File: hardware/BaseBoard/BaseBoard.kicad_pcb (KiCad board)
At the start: 2 copper layers, 81.3 x 106.7 mm, 89 parts, among them IC1 PCF8574RGTR, J1-ESP1 ESP-1-L, J1-ESP2 ESP-1-L, J1-ESP3 ESP-1-L, J1-ESP4 ESP-1-L, J1-ESP5 ESP-1-L, J1-ESP6 ESP-1-L, J1-ESP7 ESP-1-L, J1-ESP8 ESP-1-L, J2-ESP1 ESP-1-R, J2-ESP2 ESP-1-R, J2-ESP3 ESP-1-R, J2-ESP4 ESP-1-R, J2-ESP5 ESP-1-R, J2-ESP6 ESP-1-R, J2-ESP7 ESP-1-R, J2-ESP8 ESP-1-R, J3-BUS1 BUS-IN, J3-BUS2 BUS-IN, J3-BUS3 BUS-IN, J3-BUS4 BUS-IN, J3-BUS5 BUS-IN, J3-BUS6 BUS-IN, J3-BUS7 BUS-IN, J3-BUS8 BUS-IN, J4-BUS1 BUS-OUT, J4-BUS2 BUS-OUT, J4-BUS3 BUS-OUT, J4-BUS4 BUS-OUT, J4-BUS5 BUS-OUT, J4-BUS6 BUS-OUT, J4-BUS7 BUS-OUT, J4-BUS8 BUS-OUT, Q11 2N3904, Q12 AO3401A, Q21 2N3904, Q22 AO3401A, Q31 2N3904, Q32 AO3401A, Q41 2N3904, Q42 AO3401A, Q51 2N3904, Q52 AO3401A, Q61 2N3904, Q62 AO3401A, Q71 2N3904, Q72 AO3401A, Q81 2N3904, Q82 AO3401A, SW1 SW_DIP_SPSTx03, U1 AMS1117-3.3

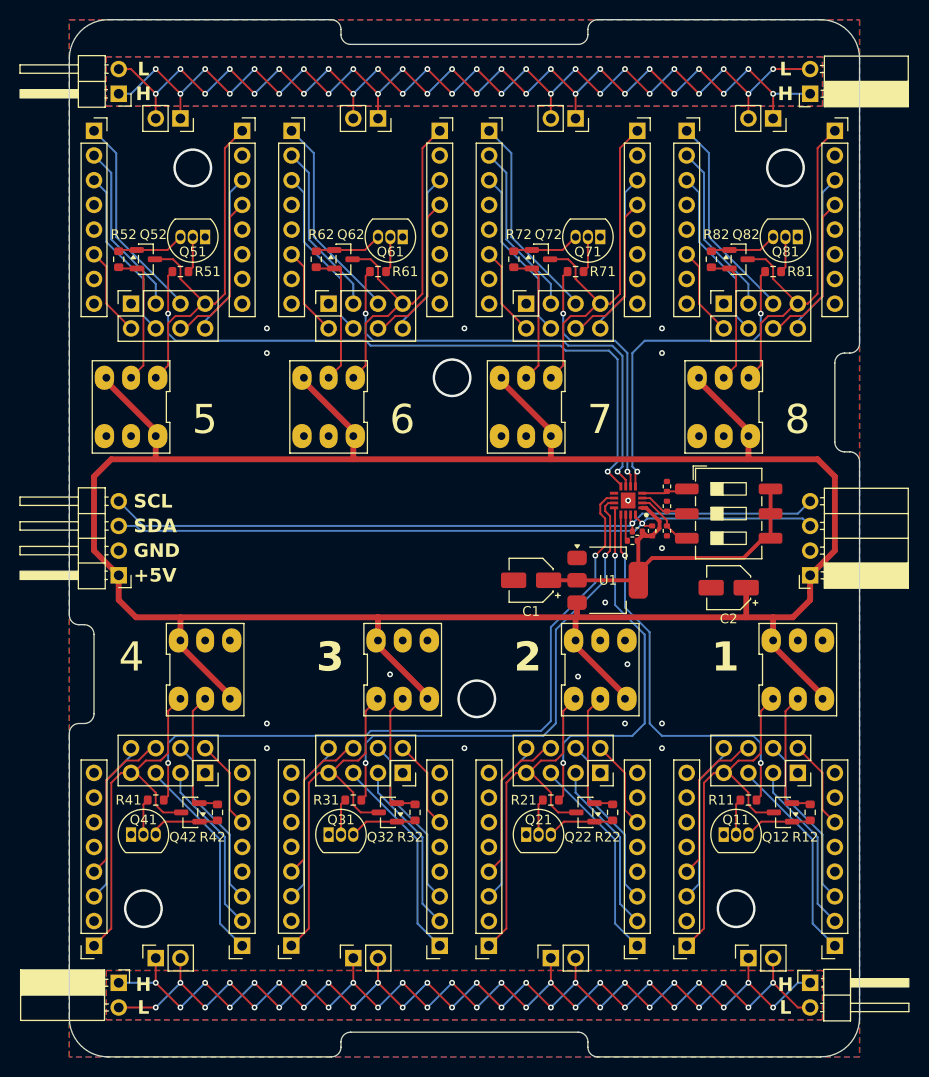
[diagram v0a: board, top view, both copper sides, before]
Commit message: Simplified BaseBoard.
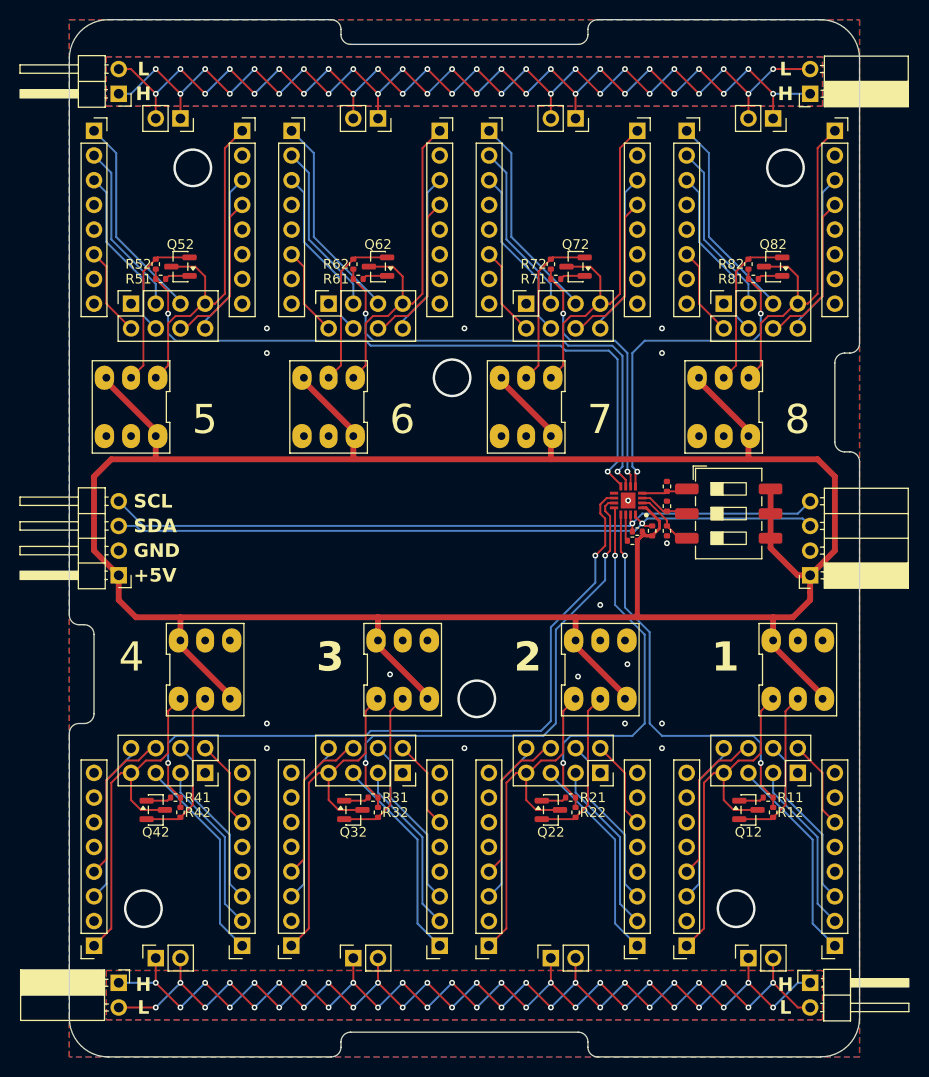
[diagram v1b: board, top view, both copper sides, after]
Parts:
- removed C1: 22µF, Capacitor_SMD:CP_Elec_4x5.3
- removed C2: 10µF, Capacitor_SMD:CP_Elec_4x5.3
- removed Q11, Q21, Q31, Q41, Q51, Q61, Q71, Q81: 2N3904, Package_TO_SOT_THT:TO-92_Inline
- removed U1: AMS1117-3.3, Package_TO_SOT_SMD:SOT-223-3_TabPin2
- R11, R21, R31, R41, R51, R61, R71, R81: value 500 -> 150; footprint Resistor_SMD:R_0603_1608Metric -> Resistor_SMD:R_0402_1005Metric
- R12, R22, R32, R42, R52, R62, R72, R82: value 500 -> 10k; footprint Resistor_SMD:R_0603_1608Metric -> Resistor_SMD:R_0402_1005Metric
- moved R52 3.84 mm to (130.8, 44.2), turned to -90 degrees
- moved R62 3.84 mm to (151.1, 44.2), turned to -90 degrees
- moved R72 3.84 mm to (171.4, 44.2), turned to -90 degrees
- moved R82 3.84 mm to (191.8, 44.2), turned to -90 degrees
- moved R12 3.81 mm to (194.3, 100.6), turned to 90 degrees
- moved R22 3.81 mm to (174.0, 100.6), turned to 90 degrees
- moved R32 3.81 mm to (153.7, 100.6), turned to 90 degrees
- moved R42 3.81 mm to (133.3, 100.6), turned to 90 degrees
- moved Q72 3.64 mm to (174.0, 44.5), turned to 180 degrees
- moved Q82 3.64 mm to (194.3, 44.5), turned to 180 degrees
- moved Q52 3.64 mm to (133.3, 44.5), turned to 180 degrees
- moved Q62 3.64 mm to (153.7, 44.5), turned to 180 degrees
- moved Q22 3.57 mm to (171.4, 100.3), turned to 0 degrees
- moved Q32 3.57 mm to (151.1, 100.3), turned to 0 degrees
- moved Q42 3.57 mm to (130.8, 100.3), turned to 0 degrees
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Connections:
- IC1 pad 1: +3V3 -> +5V
- Q12 pad 1: Net-(Q11-C) -> Net-(Q12-G)
- Q22 pad 1: Net-(Q21-C) -> Net-(Q22-G)
- Q32 pad 1: Net-(Q31-C) -> Net-(Q32-G)
- Q42 pad 1: Net-(Q41-C) -> Net-(Q42-G)
- Q52 pad 1: Net-(Q51-C) -> Net-(Q52-G)
- Q62 pad 1: Net-(Q61-C) -> Net-(Q62-G)
- Q72 pad 1: Net-(Q71-C) -> Net-(Q72-G)
- Q82 pad 1: Net-(Q81-C) -> Net-(Q82-G)
- R1 pad 2: +3V3 -> +5V
- R11 pad 1: Net-(Q11-B) -> Net-(Q12-G)
- R12 pad 2: Net-(Q11-C) -> SWPIN-ESP1
- R2 pad 2: +3V3 -> +5V
- R21 pad 1: Net-(Q21-B) -> Net-(Q22-G)
- R22 pad 2: Net-(Q21-C) -> SWPIN-ESP2
- R3 pad 2: +3V3 -> +5V
- R31 pad 1: Net-(Q31-B) -> Net-(Q32-G)
- R32 pad 2: Net-(Q31-C) -> SWPIN-ESP3
- R41 pad 1: Net-(Q41-B) -> Net-(Q42-G)
- R42 pad 2: Net-(Q41-C) -> SWPIN-ESP4
- R51 pad 1: Net-(Q51-B) -> Net-(Q52-G)
- R52 pad 2: Net-(Q51-C) -> SWPIN-ESP5
- R61 pad 1: Net-(Q61-B) -> Net-(Q62-G)
- R62 pad 2: Net-(Q61-C) -> SWPIN-ESP6
- R71 pad 1: Net-(Q71-B) -> Net-(Q72-G)
- R72 pad 2: Net-(Q71-C) -> SWPIN-ESP7
- R81 pad 1: Net-(Q81-B) -> Net-(Q82-G)
- R82 pad 2: Net-(Q81-C) -> SWPIN-ESP8
- SW1 pad 4: +3V3 -> +5V
- SW1 pad 5: +3V3 -> +5V
- SW1 pad 6: +3V3 -> +5V
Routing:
- net +3V3: track 42.6 -> 0.00 mm
- net +5V: track 266.4 -> 289.2 mm
- net Net-(Q41-C): track 7.25 -> 0.00 mm
- net Net-(Q71-C): track 6.96 -> 0.00 mm
- net Net-(Q21-C): track 6.96 -> 0.00 mm
- net Net-(Q61-C): track 6.96 -> 0.00 mm
- net Net-(Q51-C): track 6.96 -> 0.00 mm
- net Net-(Q11-C): track 6.96 -> 0.00 mm
- net Net-(Q81-C): track 6.96 -> 0.00 mm
- net Net-(Q31-C): track 6.96 -> 0.00 mm
- net Net-(Q41-B): track 3.74 -> 0.00 mm
- net Net-(Q81-B): track 3.74 -> 0.00 mm
- net Net-(Q31-B): track 3.74 -> 0.00 mm
- net Net-(Q21-B): track 3.74 -> 0.00 mm
- net Net-(Q11-B): track 3.74 -> 0.00 mm
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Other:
- board text added: "COMChallange Baseboard v1.1 github.com/raphweb"
- board text removed: "COMChallange Baseboard v1.1 - github.com/raphweb"

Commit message: Minor BaseBoard updates.
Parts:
- added R7: 50, Resistor_SMD:R_0603_1608Metric, F.Cu at (181.6, 74.2)
- renumbered Q12 to Q1, Q22 to Q2, Q32 to Q3, Q42 to Q4, Q52 to Q5, Q62 to Q6, Q72 to Q7, Q82 to Q8
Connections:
- IC1 pad 1: +5V -> +5VSwitching
- R1 pad 2: +5V -> +5VSwitching
- R2 pad 2: +5V -> +5VSwitching
- R3 pad 2: +5V -> +5VSwitching
- SW1 pad 4: +5V -> +5VSwitching
- SW1 pad 5: +5V -> +5VSwitching
- SW1 pad 6: +5V -> +5VSwitching
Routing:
- net +5VSwitching: track 0.00 -> 27.5 mm
- net +5V: track 289.2 -> 267.3 mm

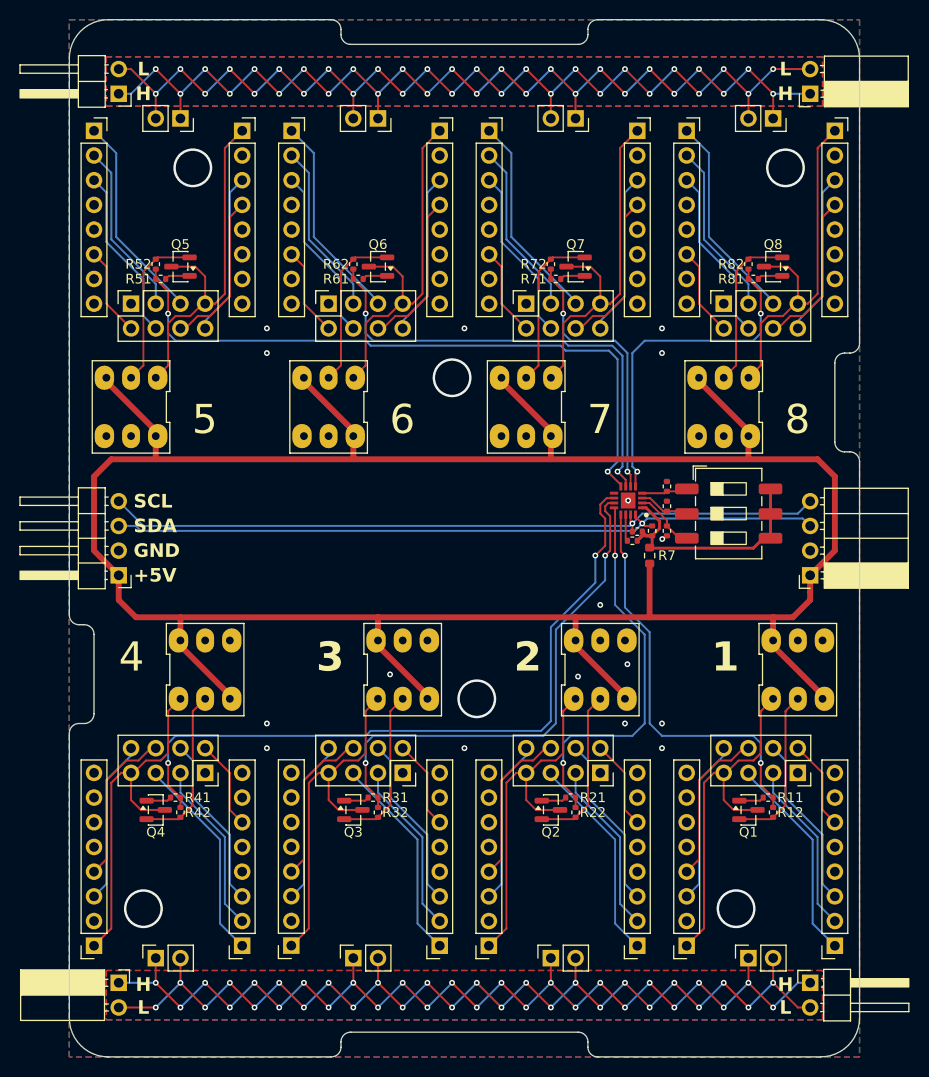
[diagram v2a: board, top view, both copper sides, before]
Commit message: Larger resistors and more GND vias.
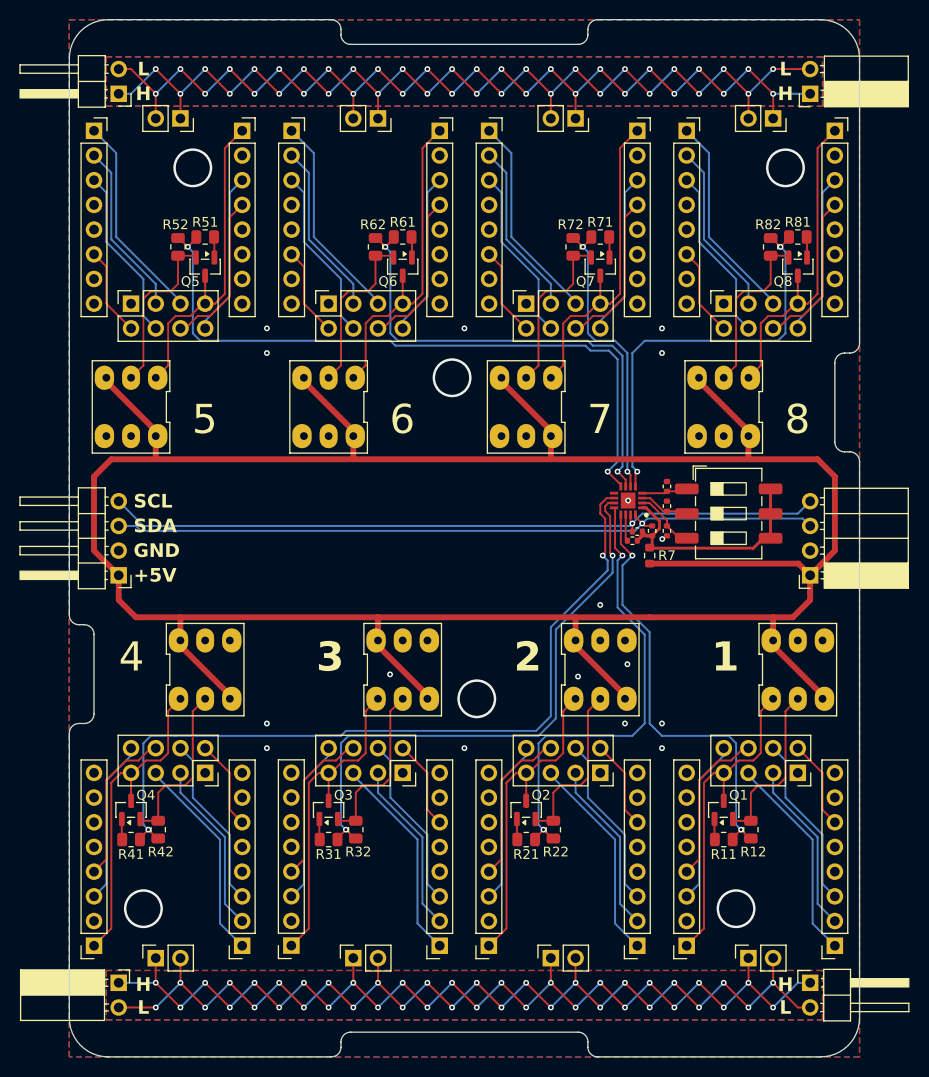
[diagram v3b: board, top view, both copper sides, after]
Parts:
- R11, R12, R21, R22, R31, R32, R41, R42, R51, R52, R61, R62, R71, R72, R81, R82: footprint Resistor_SMD:R_0402_1005Metric -> Resistor_SMD:R_0805_2012Metric
- moved R11 6.29 mm to (189.2, 103.4)
- moved R21 6.29 mm to (168.9, 103.4)
- moved R31 6.29 mm to (148.6, 103.4)
- moved R41 6.29 mm to (128.3, 103.4)
- moved R61 6.29 mm to (156.2, 41.4)
- moved R71 6.29 mm to (176.5, 41.4)
- moved R81 6.29 mm to (196.8, 41.4)
- moved R51 6.29 mm to (135.9, 41.4)
- moved R52 2.90 mm to (133.1, 42.4), turned to 90 degrees
- moved R62 2.90 mm to (153.4, 42.4), turned to 90 degrees
- moved R72 2.90 mm to (173.7, 42.4), turned to 90 degrees
- moved R82 2.90 mm to (194.1, 42.4), turned to 90 degrees
- moved R12 2.90 mm to (192.0, 102.4), turned to -90 degrees
- moved R22 2.90 mm to (171.7, 102.4), turned to -90 degrees
- moved R32 2.90 mm to (151.4, 102.4), turned to -90 degrees
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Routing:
- net +5V: track 267.3 -> 278.8 mm
- net SWPIN-ESP2: track 39.8 -> 47.5 mm
- net SWPIN-ESP4: track 73.9 -> 81.3 mm
- net SWPIN-ESP8: track 35.2 -> 42.5 mm
- net SWPIN-ESP3: track 53.5 -> 60.6 mm
- net Net-(J2-ESP6-Pin_1): track 37.4 -> 33.6 mm
- net Net-(J2-ESP1-Pin_1): track 37.4 -> 33.6 mm
- net Net-(J2-ESP7-Pin_1): track 37.4 -> 33.6 mm
- net Net-(J2-ESP8-Pin_1): track 37.4 -> 33.6 mm
- net Net-(J2-ESP5-Pin_1): track 37.4 -> 33.6 mm
- net Net-(J2-ESP4-Pin_1): track 37.4 -> 33.6 mm
- net Net-(J2-ESP3-Pin_1): track 37.4 -> 33.6 mm
- net Net-(J2-ESP2-Pin_1): track 37.4 -> 33.6 mm
- net SWPIN-ESP1: track 42.1 -> 45.2 mm
- net SWPIN-ESP7: track 28.4 -> 30.6 mm
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
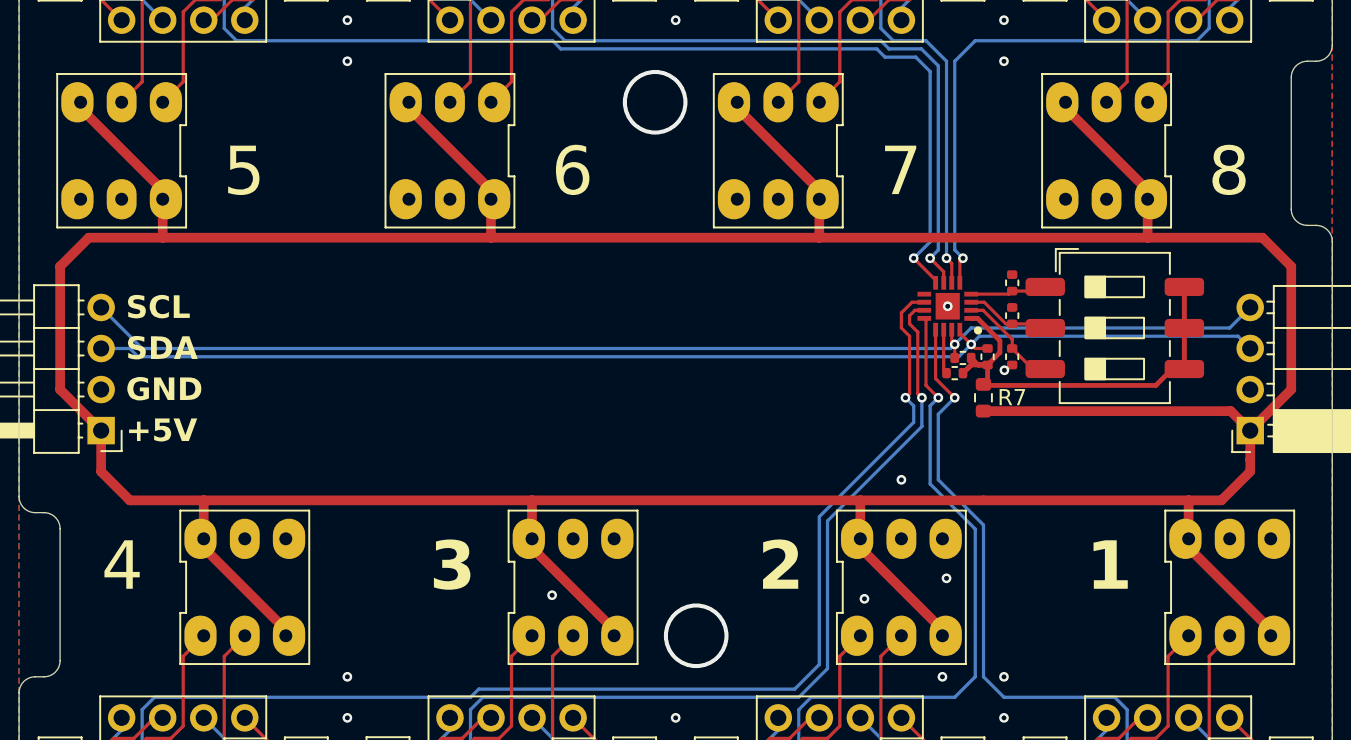
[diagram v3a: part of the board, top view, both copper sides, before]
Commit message: Added software for thumbstick test.
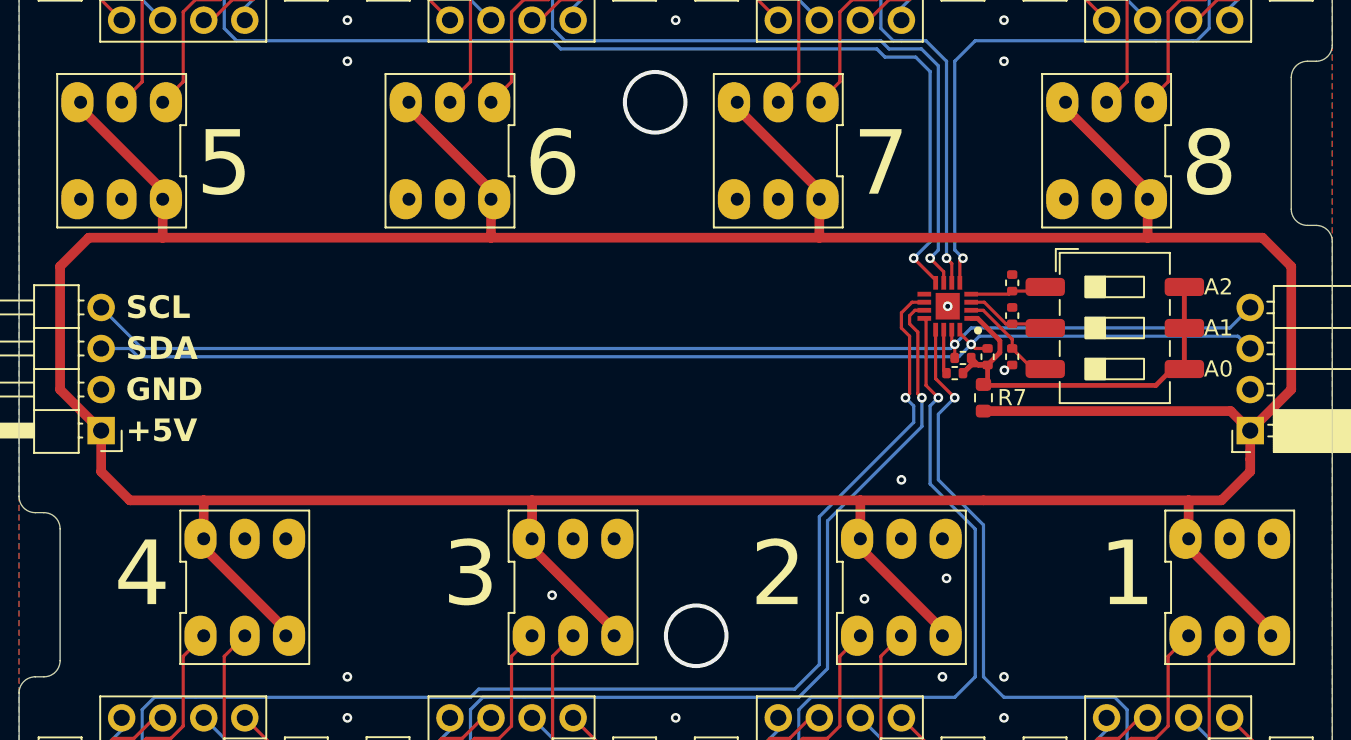
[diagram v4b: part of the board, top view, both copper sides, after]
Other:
- board text added: "A0"
- board text added: "A1"
- board text added: "A2"
